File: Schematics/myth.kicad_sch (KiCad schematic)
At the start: 137 parts, among them J1 Conn_01x08_Male, J10 Conn_01x04_Male, J11 Conn_02x01, J2 Conn_01x08_Male, J3 Conn_01x08_Male, J4 Conn_01x08_Male, J5 Conn_01x08_Male, J6 Conn_01x08_Male, J8 Conn_01x08_Male, J9 Conn_01x04_Male, U1 74AHC02, U10 74HC595, U11 74HC165, U12 74AHC08, U13 74HC238, U14 74HC238, U15 74HC238, U16 4002, U17 74HC32, U18 74AHC273, U19 74LS32, U2 74AHC273, U20 CD4532BE, U21 74AHC138, U22 74AHC04, U23 74AHC138, U24 74HC238, U25 74HC238, U26 74LS32, U27 4078, U28 74AHC244, U29 74AHC138, U3 74HC74, U30 74AHC138, U31 4075, U32 74AHC02, U33 74AHC138, U34 74HC238, U35 74AHC138, U36 74HC163, U37 74AHC574, U38 74HC238, U39 74HC32, U4 74AHC04, U40 74AHC04, U41 74AHC574, U42 74HC74, U43 74AHC273, U44 74HC283, U45 74HC283, U46 74AHC273, U47 74HC02, U48 74HC157, U49 74HC157, U5 74AHC04, U50 74AHC244, U51 74AHC04, U52 74HC283, U53 74HC193, U54 74HC193, U55 74HC193, U56 74HC193, U57 74AHC273, U58 74HC193, U59 74HC193, U6 74AHC08, U60 74AHC244, U61 74LS32, U62 4078, U63 74LS08, U64 74LS21, U65 74AHC04, U66 74AHC273, U67 74HC157, U68 74HC157, U69 74AHC574, U7 74HC00, U71 74LS257, U72 74LS257, U73 74HC04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

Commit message: Add hardware interrupt system
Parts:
- added U70, U80: 74HC157, Package_DIP:DIP-16_W7.62mm_Socket_LongPads, symbol 74xx:74LS157
- added U99: 4078, Package_DIP:DIP-14_W7.62mm_Socket_LongPads, symbol 4xxx_IEEE:4078
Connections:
- net +5V: now also U70.16 (VCC), U70.6 (I1b), U80.16 (VCC), U99.14 (Vdd); no longer U3.10 (~{S}), U3.13 (~{R})
- net C5: now also U99.10
- net C6: now also U99.11
- net C7: now also U99.12
- net CLOSE: now also U73.3
- net DB0: now also U80.2 (I0a); no longer U2.3 (D0)
- net DB1: now also U80.5 (I0b); no longer U2.4 (D1)
- net DB2: now also U80.11 (I0c); no longer U2.7 (D2)
- net DB3: now also U80.14 (I0d); no longer U2.8 (D3)
- net DB4: now also U70.2 (I0a); no longer U2.13 (D4)
- net DB5: now also U70.5 (I0b); no longer U2.14 (D5)
- net DB6: now also U70.11 (I0c); no longer U2.17 (D6)
- net DB7: now also U70.14 (I0d); no longer U2.18 (D7)
- net GET: now also U40.6; no longer U8.6
- net GETPUT: now also U7.1; no longer U8.4
- net GND: now also U70.10 (I1c), U70.13 (I1d), U70.15 (E), U70.3 (I1a), U70.8 (GND), U80.10 (I1c), U80.13 (I1d), U80.15 (E), U80.3 (I1a), U80.6 (I1b), U80.8 (GND), U99.2, U99.3, U99.4, U99.5, U99.7 (Vss), U99.9; no longer U40.5, U63.10, U63.9, U7.1, U7.2, U73.3
- net ~{PH0}: now also U8.5
- net at U3.9 (Q): now also U63.9
- net at U5.2: now also U7.2; no longer U8.5
- net ~{IRQ}: now reaches J4.1 (Pin_1)
- net ~{IRQ}: now also U8.4
- net at U63.8: now also U70.1 (S), U80.1 (S)
- net ~{GET}: now reaches U7.3
- net ~{GET}: now also U40.5
- net ~{CLOSE}: now reaches U73.4
- net ~{CLOSE}: now also U3.13 (~{R})
- new net: U3.10 (~{S}), U8.6
- new net FREE: U63.10, U99.1
- new net IRQ0: U2.3 (D0), U80.4 (Za)
- new net IRQ1: U2.4 (D1), U80.7 (Zb)
- new net IRQ2: U2.7 (D2), U80.9 (Zc)
- new net IRQ3: U2.8 (D3), U80.12 (Zd)
- new net IRQ4: U2.13 (D4), U70.4 (Za)
- new net IRQ5: U2.14 (D5), U70.7 (Zb)
- new net IRQ6: U2.17 (D6), U70.9 (Zc)
- new net IRQ7: U2.18 (D7), U70.12 (Zd)
- no-connect marks 71 -> 68
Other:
- note added: "FREE signals that code execution is outside the TRAP region (pages 0-31). Intererrupts are enabled, iff this is the case"
- note added: "If interrupts are enabled (code pages >31), then an IRQ signal injects a TRAP call to page zero. The handler code at that page figures out who sent the interrupt using the IO subsystem and then manages the request. In this way, ~{RES} is also a kind of interrupt."
- note added: "Selected state output is hard-coded TRAP to page zero"
- moved on the sheet: U1A, U3B, U40C, U4B, U4D, U5A, U5D, U63C, U73B, U73C, U7A, U7C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

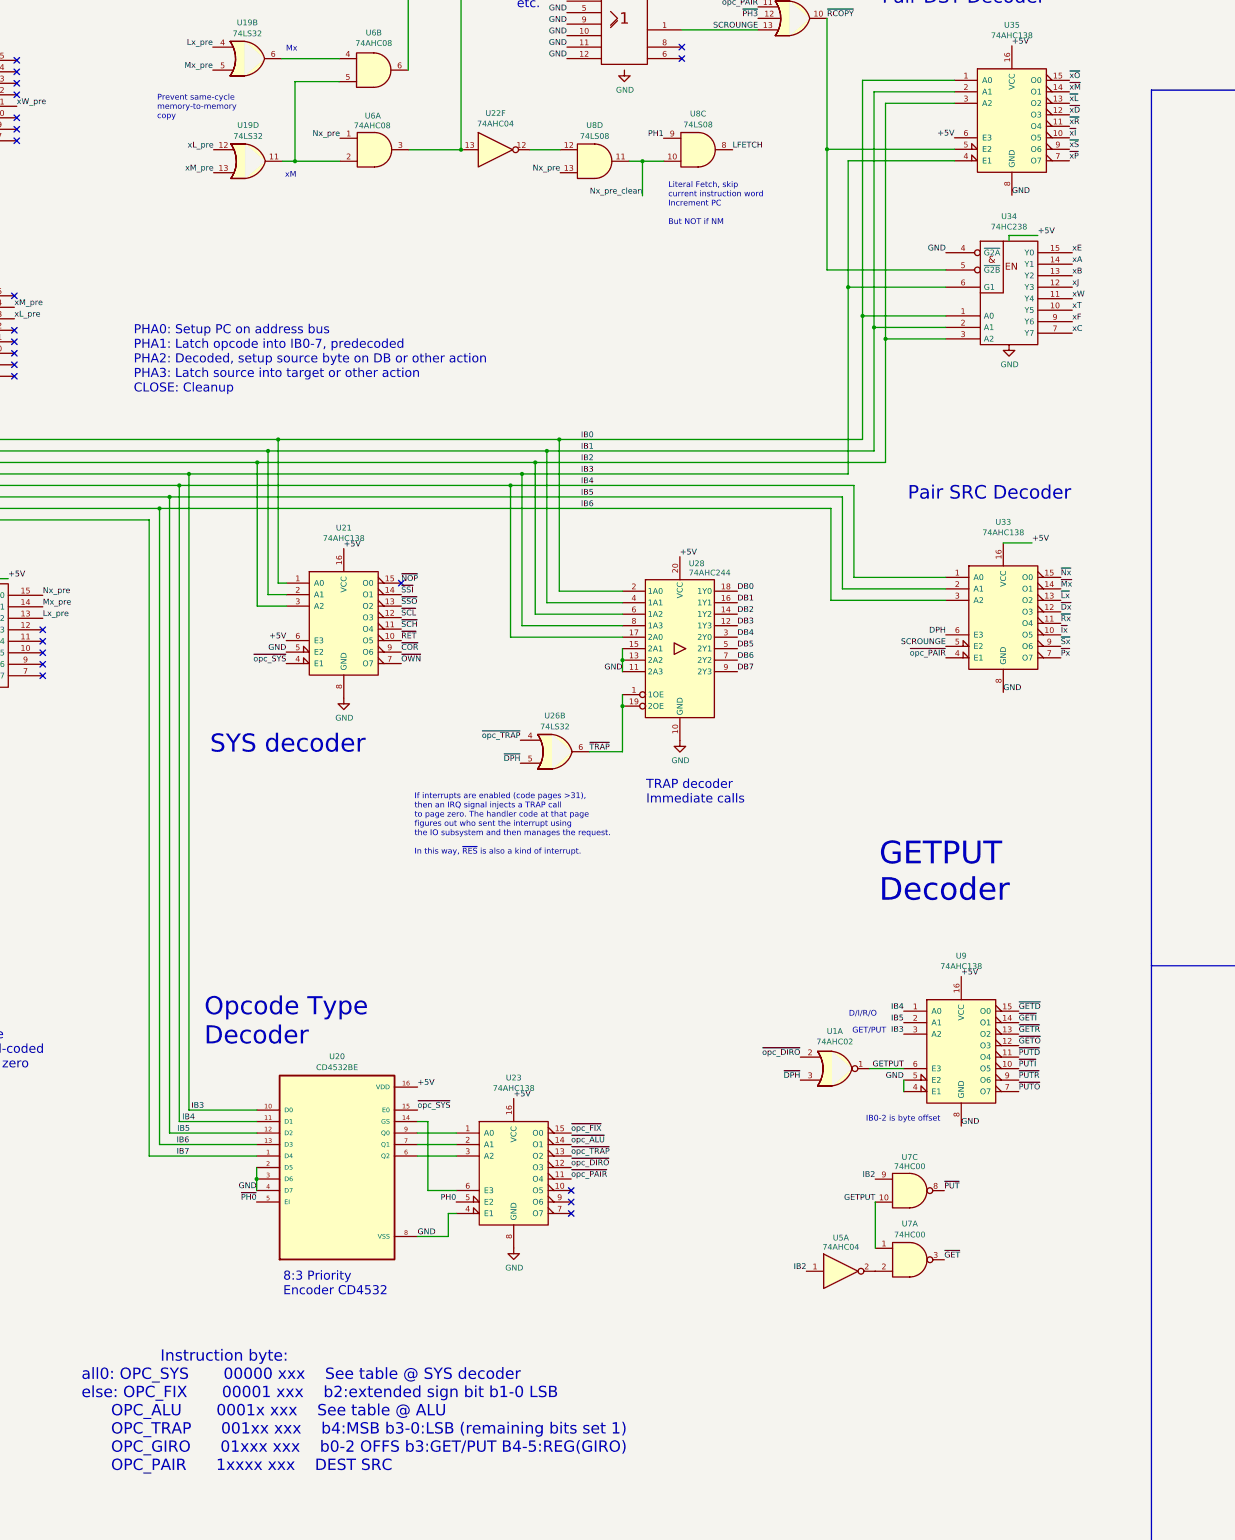
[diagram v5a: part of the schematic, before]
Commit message: Add work on automatically generating HTML docs
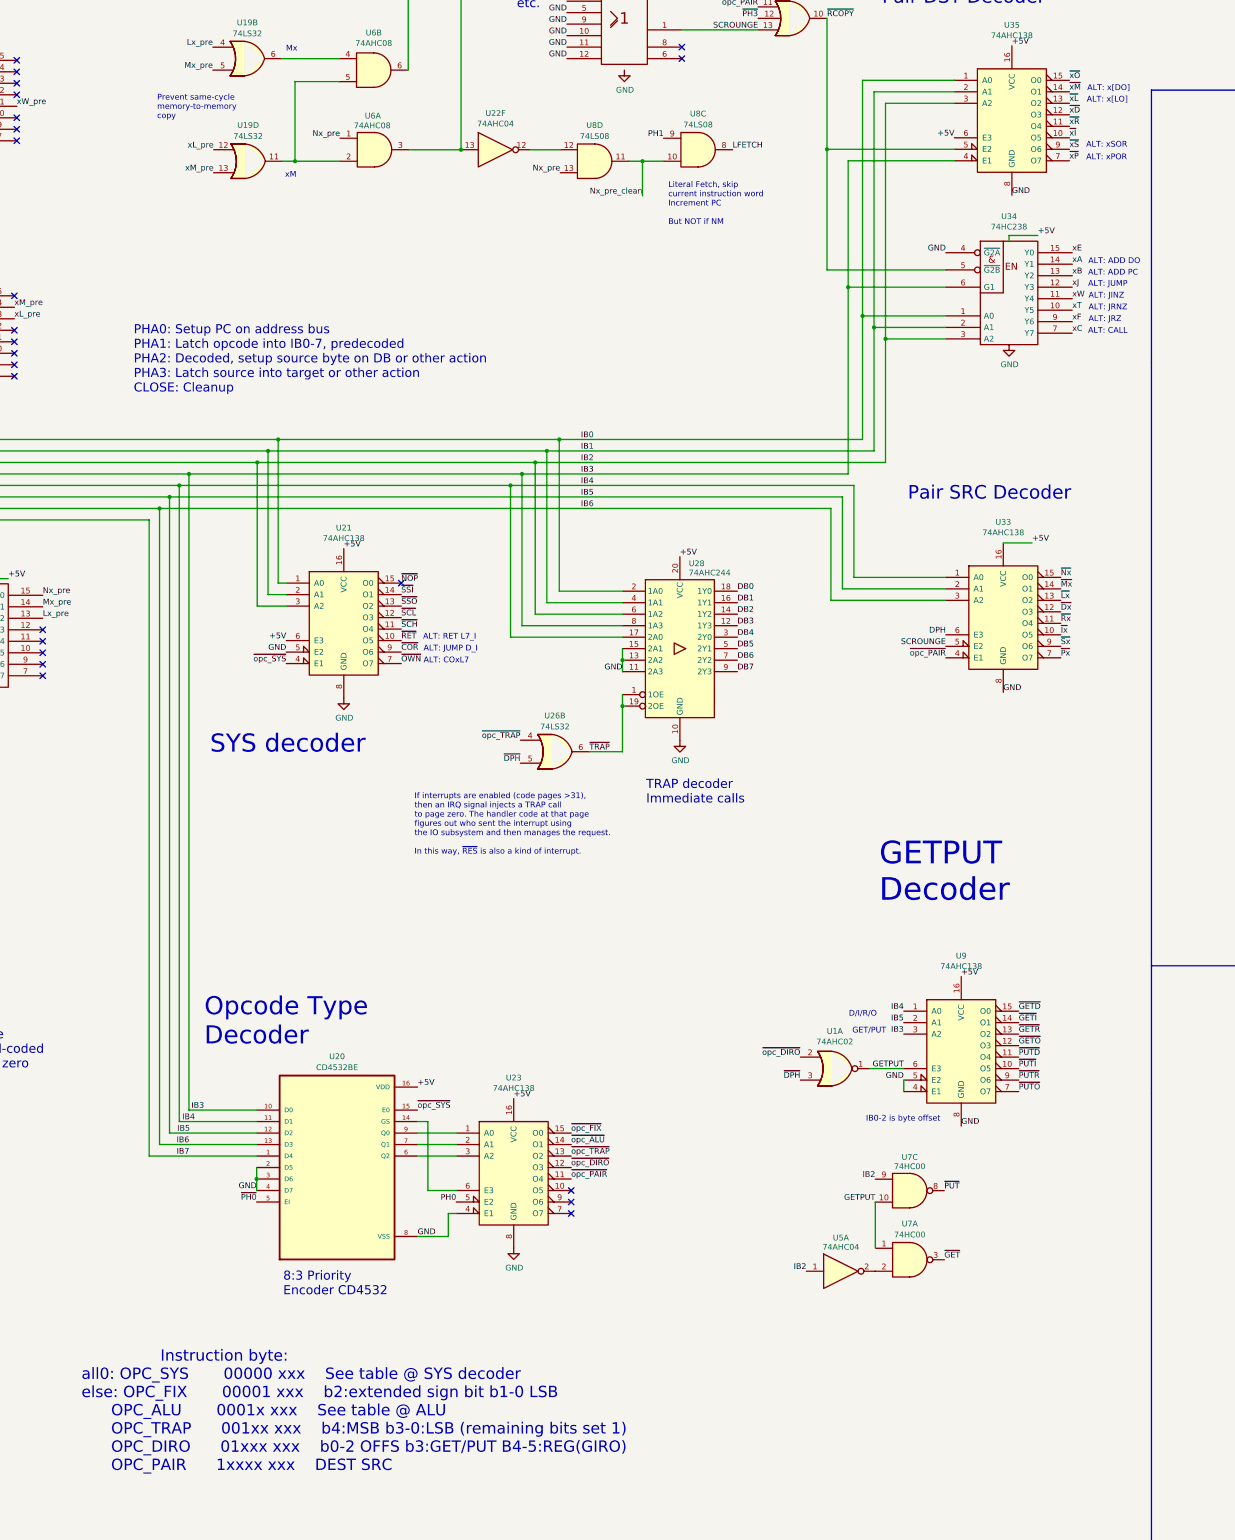
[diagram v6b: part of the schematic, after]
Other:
- note added: "ALT: ADD DO"
- note added: "ALT: ADD PC"
- note added: "ALT: CALL"
- note added: "ALT: COxL7"
- note added: "ALT: JINZ"
- note added: "ALT: JRNZ"
- note added: "ALT: JRZ"
- note added: "ALT: JUMP"
- note added: "ALT: JUMP D_I"
- note added: "ALT: RET L7_I"
- note added: "ALT: xPOR"
- note added: "ALT: xSOR"
- note added: "ALT: x[DO]"
- note added: "ALT: x[LO]"
- note added: "Instruction byte: all0: OPC_SYS 00000 xxx See table @ SYS decoder else: OPC_FIX 00001 xxx b2:extended sign bit b1-0 LSB OPC_ALU 0001x xxx See table @ ALU OPC_TRAP 001xx xxx b4:MSB b3-0:LSB (remaining bits set 1) OPC_DIRO 01xxx xxx b0-2 OFFS b3:GET/PUT B4-5:REG(GIRO) OPC_PAIR 1xxxx xxx DEST SRC"
- note removed: "Instruction byte: all0: OPC_SYS 00000 xxx See table @ SYS decoder else: OPC_FIX 00001 xxx b2:extended sign bit b1-0 LSB OPC_ALU 0001x xxx See table @ ALU OPC_TRAP 001xx xxx b4:MSB b3-0:LSB (remaining bits set 1) OPC_GIRO 01xxx xxx b0-2 OFFS b3:GET/PUT B4-5:REG(GIRO) OPC_PAIR 1xxxx xxx DEST SRC"
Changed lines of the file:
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@@
+		)
+	)
+	(text "ALT: JRNZ"
+		(exclude_from_sim no)
+		(at 368.5148 314.8425 0)
+		(effects
+			(font
+				(size 1.27 1.27)
+			)
+			(justify left bottom)
 		)
 	)
@@
 		)
 	)
+	(text "ALT: COxL7"
+		(exclude_from_sim no)
+		(at 221.5516 392.8621 0)
+		(effects
+			(font
+				(size 1.27 1.27)
+			)
+			(justify left bottom)
+		)
+	)
 	(text "ALU\n opcode"
 		(exclude_from_sim no)
@@
 		)
 	)
+	(text "ALT: xSOR"
+		(exclude_from_sim no)
+		(at 367.9979 278.8966 0)
+		(effects
+			(font
+				(size 1.27 1.27)
+			)
+			(justify left bottom)
+		)
+	)
 	(text "Pair SRC Decoder"
 		(exclude_from_sim no)
@@
 		)
 	)
+	(text "ALT: ADD PC"
+		(exclude_from_sim no)
+		(at 368.4151 307.1688 0)
+		(effects
+			(font
+				(size 1.27 1.27)
+			)
+			(justify left bottom)
+		)
+	)
 	(text "W=While\nIntended to\npost decrement\nfor either case"
 		(exclude_from_sim no)
@@
 		)
 	)
+	(text "ALT: xPOR"
+		(exclude_from_sim no)
+		(at 367.9979 281.6772 0)
+		(effects
+			(font
+				(size 1.27 1.27)
+			)
+			(justify left bottom)
+		)
+	)
 	(text "HI7 switches\nbetween RAM and ROM"
 		(exclude_from_sim no)
@@
 		)
 	)
-	(text "                Instruction byte:\nall0: OPC_SYS       00000 xxx    See table @ SYS decoder\nelse: OPC_FIX       00001 xxx    b2:extended sign bit b1-0 LSB\n      OPC_ALU       0001x xxx    See table @ ALU\n      OPC_TRAP      001xx xxx    b4:MSB b3-0:LSB (remaining bits set 1)\n      OPC_GIRO      01xxx xxx    b0-2 OFFS b3:GET/PUT B4-5:REG(GIRO)\n      OPC_PAIR      1xxxx xxx    DEST SRC"
+	(text "                Instruction byte:\nall0: OPC_SYS       00000 xxx    See table @ SYS decoder\nelse: OPC_FIX       00001 xxx    b2:extended sign bit b1-0 LSB\n      OPC_ALU       0001x xxx    See table @ ALU\n      OPC_TRAP      001xx xxx    b4:MSB b3-0:LSB (remaining bits set 1)\n      OPC_DIRO      01xxx xxx    b0-2 OFFS b3:GET/PUT B4-5:REG(GIRO)\n      OPC_PAIR      1xxxx xxx    DEST SRC"
 		(exclude_from_sim no)
 		(at 145.9388 571.5103 0)
@@
 		)
 	)
+	(text "ALT: JUMP D_I"
+		(exclude_from_sim no)
+		(at 221.5516 390.2384 0)
+		(effects
+			(font
+				(size 1.27 1.27)
+			)
+			(justify left bottom)
+		)
+	)
 	(text "0 CLR (\"Clear\" / R:=0)\n1 IDO (\"Identity O\" / R:=O)\n2 OCR (\"Ones Complement R\" / R:=~R)\n3 OCO (\"Ones Complement O\" / R:=~O)\n4 SLR (\"Shift left R\" / R:=R<<1)\n5 SLO (\"Shift left O\" / R:=O<<1)\n6 SRR (\"Shift right R\" / R:=R>>1)\n7 SRO (\"Shift right O\" / R:=O>>1)"
 		(exclude_from_sim no)
@@
 		)
 	)
+	(text "ALT: RET L7_I"
+		(exclude_from_sim no)
+		(at 221.4381 387.6319 0)
+		(effects
+			(font
+				(size 1.27 1.27)
+			)
+			(justify left bottom)
+		)
+	)
 	(text "xM"
 		(exclude_from_sim no)
@@
 		)
 	)
+	(text "ALT: x[DO]"
+		(exclude_from_sim no)
+		(at 368.2296 266.384 0)
+		(effects
+			(font
+				(size 1.27 1.27)
+			)
+			(justify left bottom)
+		)
+	)
 	(text "Branching"
 		(exclude_from_sim no)
@@
 		)
 	)
+	(text "ALT: CALL"
+		(exclude_from_sim no)
+		(at 368.4151 320.0247 0)
+		(effects
+			(font
+				(size 1.27 1.27)
+			)
+			(justify left bottom)
+		)
+	)
 	(text "~{RES} request"
 		(exclude_from_sim no)
@@
 		)
 	)
+	(text "ALT: JUMP"
+		(exclude_from_sim no)
+		(at 368.4151 309.6603 0)
+		(effects
+			(font
+				(size 1.27 1.27)
+			)
+			(justify left bottom)
+		)
+	)
 	(text "Hard-coded:\nif bits 0-2 all 0\nreplace by 4"
 		(exclude_from_sim no)
@@
 		)
 	)
+	(text "ALT: x[LO]"
+		(exclude_from_sim no)
+		(at 368.1137 268.9328 0)
+		(effects
+			(font
+				(size 1.27 1.27)
+			)
+			(justify left bottom)
+		)
+	)
 	(text "Power"
 		(exclude_from_sim no)
@@
 		)
 	)
+	(text "ALT: ADD DO"
+		(exclude_from_sim no)
+		(at 368.4613 304.6169 0)
+		(effects
+			(font
+				(size 1.27 1.27)
+			)
+			(justify left bottom)
+		)
+	)
+	(text "ALT: JINZ"
+		(exclude_from_sim no)
+		(at 368.5148 312.2514 0)
+		(effects
+			(font
+				(size 1.27 1.27)
+			)
+			(justify left bottom)
+		)
+	)
 	(text " 8 AND (R:=R&O)\n 9 IOR (R:=R|O)\n10 EOR (R:=R^O)\n11 ADD (Add\" / R:=R+O, bits 0-7)\n12 CAR (\"Carry Bit\" / R:= Carry, 9th bit of R+O) 00h or 01h\n13 RLO (\"Flag: R less than O\" / R:= (R<O)? 0xFF:0\n14 REO (\"Flag: R equals O\" / R:= (R==O)? 0xFF:0\n15 RGO (\"Flag: R greater than O\" / R:= (R>O)? 0xFF:0\n"
 		(exclude_from_sim no)
@@
 			)
 			(justify left bottom)
+		)
+	)
+	(text "ALT: JRZ"
+		(exclude_from_sim no)
+		(at 368.5148 317.4336 0)
+		(effects
+			(font
+				(size 1.27 1.27)
+			)
+			(justify left bottom)

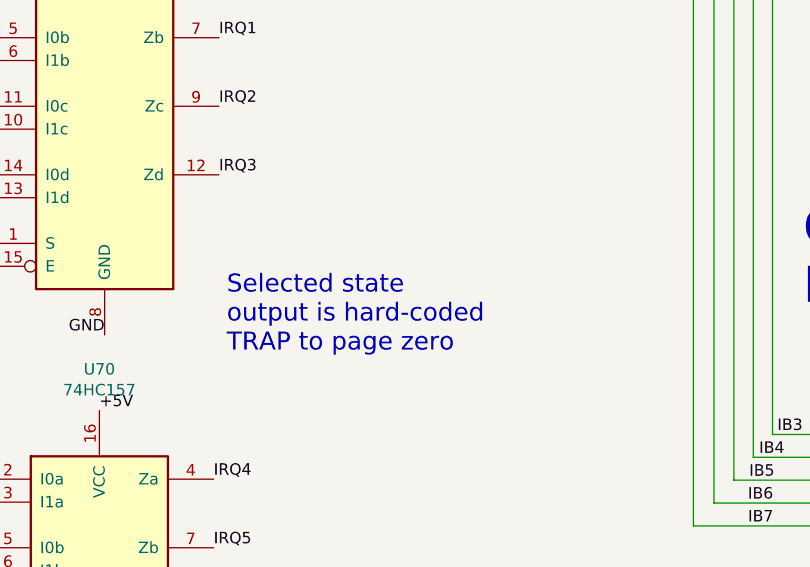
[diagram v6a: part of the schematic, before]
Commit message: Fix/add docs for scrounge opcodes
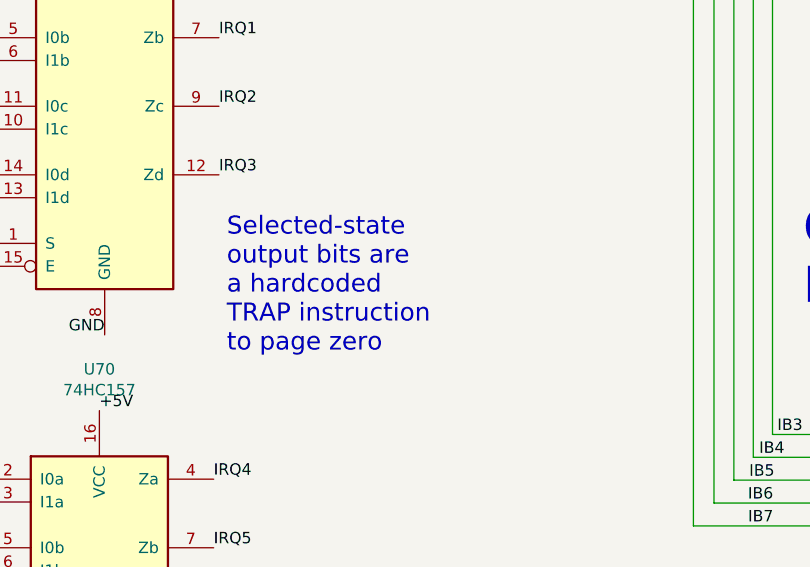
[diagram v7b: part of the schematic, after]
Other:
- note added: "Selected-state output bits are a hardcoded TRAP instruction to page zero"
- note removed: "Selected state output is hard-coded TRAP to page zero"
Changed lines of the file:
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@@
 		(comment 1 "Author: Michael Mangelsdorf")
 		(comment 2 "Project homepage: https://github.com/Dosflange/Myth")
-		(comment 3 "Rev. Step LOX (\"Frozen\")")
+		(comment 3 "Rev. Step LOX (\"Frozen 100\")")
 	)
 	(junction
@@
 		)
 	)
-	(text "Selected state\noutput is hard-coded\nTRAP to page zero"
+	(text "Selected-state\noutput bits are\na hardcoded\nTRAP instruction\nto page zero"
 		(exclude_from_sim no)
 		(at 109.0637 482.4699 0)
